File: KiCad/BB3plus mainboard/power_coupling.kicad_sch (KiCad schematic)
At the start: 17 parts, among them IC28 TLE75008ESDXUMA1, K3 RT424012, K4 RT424012, K5 RT424012, K6 RT424012, K7 RT424012, X24 77313-802-20LF, X25 77313-802-20LF, X26 TBP03R1-350-10BE, X27 77313-802-20LF

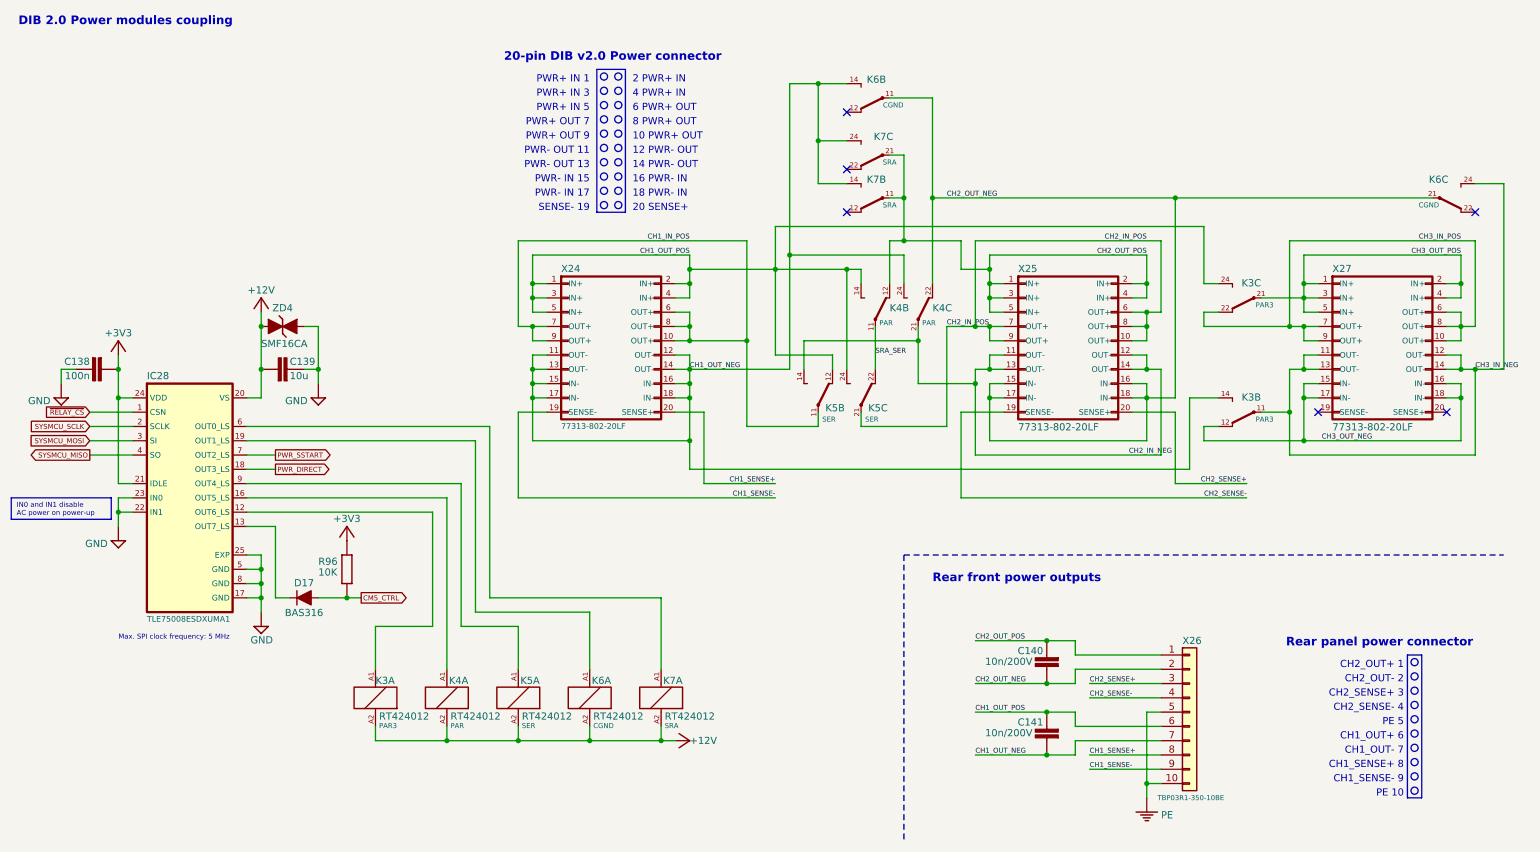
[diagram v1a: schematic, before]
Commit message: PE fault detection section updated
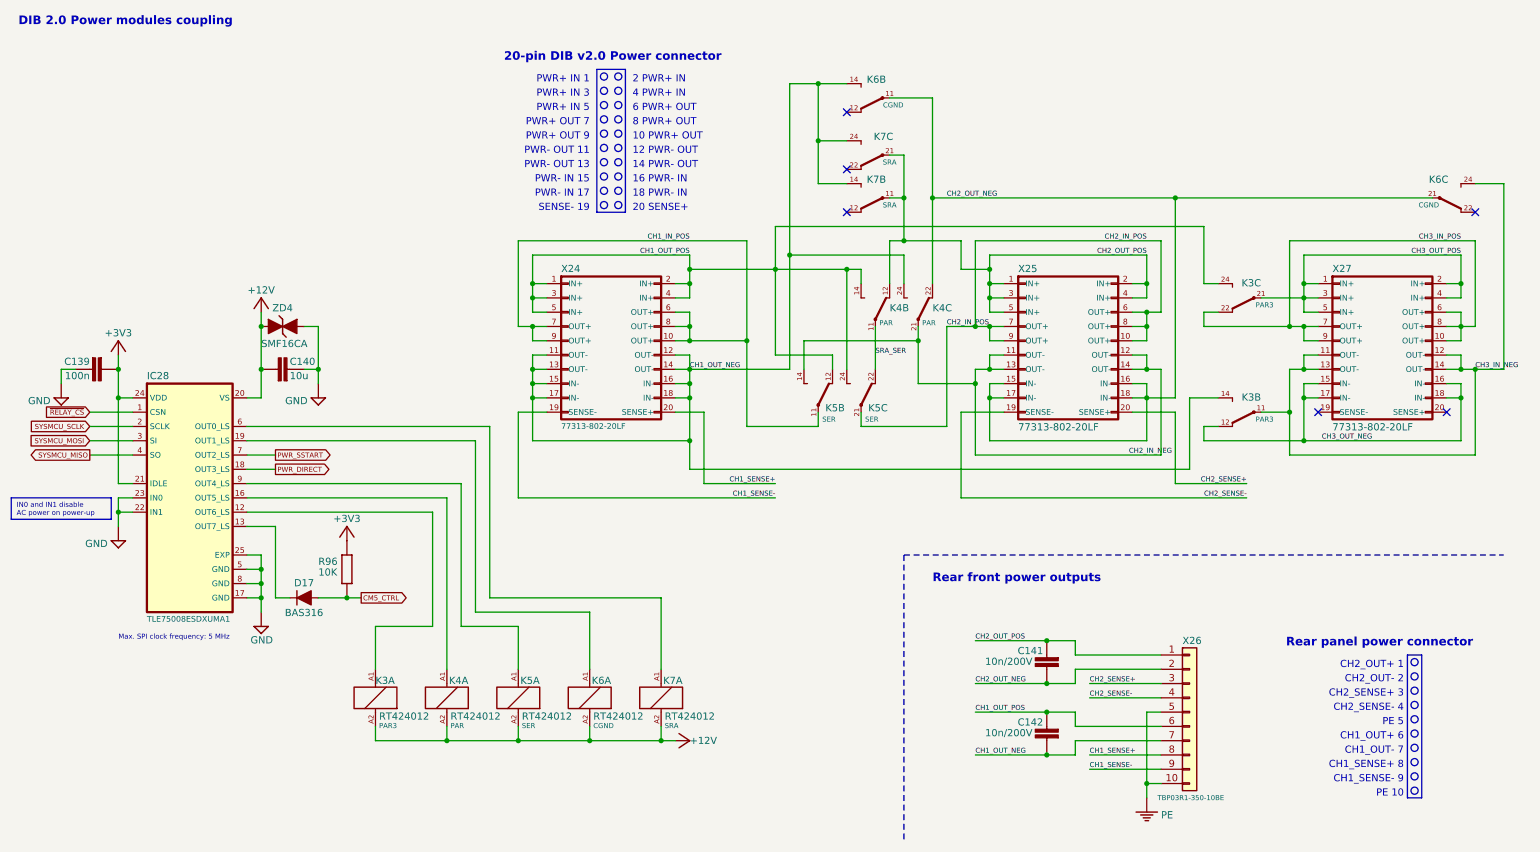
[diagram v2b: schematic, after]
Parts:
- renumbered C138 to C139, C139 to C140, C140 to C141, C141 to C142
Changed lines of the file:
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@@
 		(in_pos_files yes)
 		(dnp no)
-		(property "Reference" "C138"
+		(property "Reference" "C139"
 			(at 30.48 78.105 90)
 			(show_name no)
@@
 			(project "BB3plus mainboard"
 				(path "/1df84e4f-233a-4f72-9418-c0020706bb76/bb7e7620-5970-4f17-83aa-0b2c666475d0"
-					(reference "C138")
+					(reference "C139")
 					(unit 1)
 				)
@@
 		(in_pos_files yes)
 		(dnp no)
-		(property "Reference" "#SUPPLY0114"
+		(property "Reference" "#SUPPLY0117"
 			(at 60.96 124.46 0)
 			(hide yes)
@@
 			(project "BB3plus mainboard"
 				(path "/1df84e4f-233a-4f72-9418-c0020706bb76/bb7e7620-5970-4f17-83aa-0b2c666475d0"
-					(reference "#SUPPLY0114")
+					(reference "#SUPPLY0117")
 					(unit 1)
 				)
@@
 		(in_pos_files yes)
 		(dnp no)
-		(property "Reference" "C141"
+		(property "Reference" "C142"
 			(at 200.025 142.24 0)
 			(show_name no)
@@
 			(project "BB3plus mainboard"
 				(path "/1df84e4f-233a-4f72-9418-c0020706bb76/bb7e7620-5970-4f17-83aa-0b2c666475d0"
-					(reference "C141")
+					(reference "C142")
 					(unit 1)
 				)
@@
 		(in_pos_files yes)
 		(dnp no)
-		(property "Reference" "#SUPPLY0112"
+		(property "Reference" "#SUPPLY0115"
 			(at 35.56 109.22 0)
 			(hide yes)
@@
 			(project "BB3plus mainboard"
 				(path "/1df84e4f-233a-4f72-9418-c0020706bb76/bb7e7620-5970-4f17-83aa-0b2c666475d0"
-					(reference "#SUPPLY0112")
+					(reference "#SUPPLY0115")
 					(unit 1)
 				)
@@
 		(in_pos_files yes)
 		(dnp no)
-		(property "Reference" "#SUPPLY0116"
+		(property "Reference" "#SUPPLY0119"
 			(at 137.16 144.78 0)
 			(hide yes)
@@
 			(project "BB3plus mainboard"
 				(path "/1df84e4f-233a-4f72-9418-c0020706bb76/bb7e7620-5970-4f17-83aa-0b2c666475d0"
-					(reference "#SUPPLY0116")
+					(reference "#SUPPLY0119")
 					(unit 1)
 				)
@@
 		(in_pos_files yes)
 		(dnp no)
-		(property "Reference" "#SUPPLY0113"
+		(property "Reference" "#SUPPLY0116"
 			(at 60.96 66.04 0)
 			(hide yes)
@@
 			(project "BB3plus mainboard"
 				(path "/1df84e4f-233a-4f72-9418-c0020706bb76/bb7e7620-5970-4f17-83aa-0b2c666475d0"
-					(reference "#SUPPLY0113")
+					(reference "#SUPPLY0116")
 					(unit 1)
 				)
@@
 		(in_pos_files yes)
 		(dnp no)
-		(property "Reference" "#SUPPLY0111"
+		(property "Reference" "#SUPPLY0114"
 			(at 25.4 83.82 0)
 			(hide yes)
@@
 			(project "BB3plus mainboard"
 				(path "/1df84e4f-233a-4f72-9418-c0020706bb76/bb7e7620-5970-4f17-83aa-0b2c666475d0"
-					(reference "#SUPPLY0111")
+					(reference "#SUPPLY0114")
 					(unit 1)
 				)
@@
 		(in_pos_files yes)
 		(dnp no)
-		(property "Reference" "#SUPPLY0115"
+		(property "Reference" "#SUPPLY0118"
 			(at 71.12 83.82 0)
 			(hide yes)
@@
 			(project "BB3plus mainboard"
 				(path "/1df84e4f-233a-4f72-9418-c0020706bb76/bb7e7620-5970-4f17-83aa-0b2c666475d0"
-					(reference "#SUPPLY0115")
+					(reference "#SUPPLY0118")
 					(unit 1)
 				)
@@
 		(in_pos_files yes)
 		(dnp no)
-		(property "Reference" "C140"
+		(property "Reference" "C141"
 			(at 200.025 129.54 0)
 			(show_name no)
@@
 			(project "BB3plus mainboard"
 				(path "/1df84e4f-233a-4f72-9418-c0020706bb76/bb7e7620-5970-4f17-83aa-0b2c666475d0"
-					(reference "C140")
+					(reference "C141")
 					(unit 1)
 				)
@@
 		(in_pos_files yes)
 		(dnp no)
-		(property "Reference" "C139"
+		(property "Reference" "C140"
 			(at 66.04 78.105 90)
 			(show_name no)
@@
 			(project "BB3plus mainboard"
 				(path "/1df84e4f-233a-4f72-9418-c0020706bb76/bb7e7620-5970-4f17-83aa-0b2c666475d0"
-					(reference "C139")
+					(reference "C140")
 					(unit 1)
 				)

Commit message: Various small changes
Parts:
- X25: renamed from X24; value 77313-802-20LF -> PH2-20-UA; LCSC C3327336 -> C3327060; Mouser 649-77313-802-20LF -> 737-PH2-20-UA; TME ZL202-20G -> TSW-110-07-L-D
- X26: renamed from X25; value 77313-802-20LF -> PH2-20-UA; LCSC C3327336 -> C3327060; Mouser 649-77313-802-20LF -> 737-PH2-20-UA; TME ZL202-20G -> TSW-110-07-L-D
- X28: renamed from X27; value 77313-802-20LF -> PH2-20-UA; LCSC C3327336 -> C3327060; Mouser 649-77313-802-20LF -> 737-PH2-20-UA; TME ZL202-20G -> TSW-110-07-L-D
- renumbered X26 to X27
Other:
- note added: "(Slots #1 and #2 only)"
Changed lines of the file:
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@@
 	(title_block
 		(title "${project_name}")
-		(date "2026-10-09")
+		(date "2026-10-12")
 		(rev "${project_version}")
 		(company "${project_creator}")
@@
 		)
 	)
+	(text "(Slots #1 and #2 only)"
+		(exclude_from_sim no)
+		(at 248.92 127.635 0)
+		(effects
+			(font
+				(size 1.27 1.27)
+				(color 255 0 255 1)
+			)
+			(justify left bottom)
+		)
+	)
 	(text "8 PWR+ OUT"
 		(exclude_from_sim no)
@@
 	(text "Rear panel power connector"
 		(exclude_from_sim no)
-		(at 243.205 128.27 0)
+		(at 243.205 125.095 0)
 		(effects
 			(font
@@
 	)
 	(junction
-		(at 276.86 78.74)
+		(at 281.94 78.74)
 		(diameter 0)
 		(color 0 0 0 0)
@@
 	)
 	(no_connect
-		(at 248.92 86.36)
-	)
-	(no_connect
 		(at 165.1 43.18)
 	)
 	(no_connect
-		(at 165.1 50.8)
+		(at 248.92 86.36)
 	)
 	(no_connect
 		(at 271.78 86.36)
 	)
+	(no_connect
+		(at 165.1 50.8)
+	)
 	(wire
 		(pts
@@
 	(wire
 		(pts
-			(xy 276.86 78.74) (xy 276.86 93.98)
+			(xy 281.94 78.74) (xy 281.94 93.98)
 		)
 		(stroke
@@
 	(wire
 		(pts
-			(xy 276.86 78.74) (xy 281.94 78.74)
-		)
-		(stroke
-			(width 0)
-			(type default)
-		)
-	)
-	(wire
-		(pts
 			(xy 60.96 71.12) (xy 60.96 78.74)
 		)
@@
 	(wire
 		(pts
-			(xy 243.84 93.98) (xy 276.86 93.98)
+			(xy 243.84 93.98) (xy 281.94 93.98)
 		)
 		(stroke
@@
 	(wire
 		(pts
-			(xy 274.32 78.74) (xy 276.86 78.74)
+			(xy 274.32 78.74) (xy 281.94 78.74)
 		)
 		(stroke
@@
 		)
 	)
-	(label "CH3_IN_NEG"
-		(at 276.86 78.74 0)
-		(effects
-			(font
-				(size 0.889 0.889)
-			)
-			(justify left bottom)
-		)
-	)
 	(label "SRA_SER"
 		(at 170.18 76.2 0)
@@
 		)
 	)
+	(label "CH3_IN_NEG"
+		(at 251.46 93.98 0)
+		(effects
+			(font
+				(size 0.889 0.889)
+			)
+			(justify left bottom)
+		)
+	)
 	(label "CH1_SENSE-"
 		(at 208.28 149.86 0)
@@
 	)
 	(label "CH3_OUT_NEG"
-		(at 249.555 91.44 0)
+		(at 251.46 91.44 0)
 		(effects
 			(font
@@
 		(in_pos_files yes)
 		(dnp no)
-		(property "Reference" "X25"
+		(property "Reference" "X26"
 			(at 195.58 61.595 0)
 			(show_name no)
@@
 			)
 		)
-		(property "Value" "77313-802-20LF"
+		(property "Value" "PH2-20-UA"
 			(at 195.58 88.265 0)
 			(show_name no)
@@
 			(effects
 				(font
-					(size 1.27 1.27)
+					(size 1.016 1.016)
 				)
 				(justify left top)
@@
 			)
 		)
-		(property "Mouser" "649-77313-802-20LF"
+		(property "Mouser" "737-PH2-20-UA"
 			(at 193.04 99.06 0)
 			(hide yes)
@@
 			)
 		)
-		(property "TME" "ZL202-20G"
+		(property "TME" "TSW-110-07-L-D"
 			(at 193.04 101.6 0)
 			(hide yes)
@@
 			)
 		)
-		(property "LCSC" "C3327336"
+		(property "LCSC" "C3327060"
 			(at 193.04 104.14 0)
 			(hide yes)
@@
 			(project "BB3plus mainboard"
 				(path "/1df84e4f-233a-4f72-9418-c0020706bb76/bb7e7620-5970-4f17-83aa-0b2c666475d0"
-					(reference "X25")
+					(reference "X26")
 					(unit 1)
 				)
@@
 		(in_pos_files yes)
 		(dnp no)
-		(property "Reference" "X26"
+		(property "Reference" "X27"
 			(at 224.79 127 0)
 			(show_name no)
@@
 			(project "BB3plus mainboard"
 				(path "/1df84e4f-233a-4f72-9418-c0020706bb76/bb7e7620-5970-4f17-83aa-0b2c666475d0"
-					(reference "X26")
+					(reference "X27")
 					(unit 1)
 				)
@@
 		(in_pos_files yes)
 		(dnp no)
-		(property "Reference" "X27"
+		(property "Reference" "X28"
 			(at 251.46 61.595 0)
 			(show_name no)
@@
 			)
 		)
-		(property "Value" "77313-802-20LF"
+		(property "Value" "PH2-20-UA"
 			(at 251.46 88.265 0)
 			(show_name no)
@@
 			(effects
 				(font
-					(size 1.27 1.27)
+					(size 1.016 1.016)
 				)
 				(justify left top)
@@
 			)
 		)
-		(property "Mouser" "649-77313-802-20LF"
+		(property "Mouser" "737-PH2-20-UA"
 			(at 248.92 99.06 0)
 			(hide yes)
@@
 			)
 		)
-		(property "TME" "ZL202-20G"
+		(property "TME" "TSW-110-07-L-D"
 			(at 248.92 101.6 0)
 			(hide yes)
@@
 			)
 		)
-		(property "LCSC" "C3327336"
+		(property "LCSC" "C3327060"
 			(at 248.92 104.14 0)
 			(hide yes)
@@
 			(project "BB3plus mainboard"
 				(path "/1df84e4f-233a-4f72-9418-c0020706bb76/bb7e7620-5970-4f17-83aa-0b2c666475d0"
-					(reference "X27")
+					(reference "X28")
 					(unit 1)
 				)
@@
 		(in_pos_files yes)
 		(dnp no)
-		(property "Reference" "X24"
+		(property "Reference" "X25"
 			(at 114.3 61.595 0)
 			(show_name no)
@@
 			)
 		)
-		(property "Value" "77313-802-20LF"
+		(property "Value" "PH2-20-UA"
 			(at 114.3 88.265 0)
 			(show_name no)
@@
 			)
 		)
-		(property "Mouser" "649-77313-802-20LF"
+		(property "Mouser" "737-PH2-20-UA"
 			(at 111.76 101.6 0)
 			(hide yes)
@@
 			)
 		)
-		(property "TME" "ZL202-20G"
+		(property "TME" "TSW-110-07-L-D"
 			(at 111.76 104.14 0)
 			(hide yes)
@@
 			)
 		)
-		(property "LCSC" "C3327336"
+		(property "LCSC" "C3327060"
 			(at 111.76 106.68 0)
 			(hide yes)
@@
 			(project "BB3plus mainboard"
 				(path "/1df84e4f-233a-4f72-9418-c0020706bb76/bb7e7620-5970-4f17-83aa-0b2c666475d0"
-					(reference "X24")
+					(reference "X25")
 					(unit 1)
 				)

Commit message: #24
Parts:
- removed D17: BAS316, PCM_EEZ_SMD:SOD-323_1P8X1P35_ONS-M, symbol PCM_EEZ_discretes:DIODE
- removed R96: 10K, PCM_EEZ_passives:R_0603_1608Metric, symbol PCM_EEZ_passives:R-EU
- renumbered C139 to C137, C140 to C138, C141 to C139, C142 to C140, IC28 to IC25
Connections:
- no-connect marks 6 -> 7
